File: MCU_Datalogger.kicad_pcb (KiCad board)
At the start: 2 copper layers, 0 parts

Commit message: setup for the 2layer PCB schematic
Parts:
- added BT1: Battery, Connector_PinHeader_2.54mm:PinHeader_1x02_P2.54mm_Vertical, F.Cu at (156.8, 101.4)
- added C1: 0.1 uF, Capacitor_SMD:C_0805_2012Metric, F.Cu at (179.1, 91.3)
- added C2: 22 pF, Capacitor_SMD:C_0805_2012Metric, F.Cu at (179.1, 94.4)
- added C3: 22 pF, Capacitor_SMD:C_0805_2012Metric, F.Cu at (179.1, 97.4)
- added C4: 0.1 uF, Capacitor_SMD:C_0805_2012Metric, F.Cu at (179.1, 100.4)
- added C5: 100 nF, Capacitor_SMD:C_0805_2012Metric, F.Cu at (179.1, 103.4)
- added D1: LED, LED_SMD:LED_0805_2012Metric, F.Cu at (183.5, 91.4)
- added D2: LED, LED_SMD:LED_0805_2012Metric, F.Cu at (183.5, 94.4)
- added H1: MountingHole, MountingHole:MountingHole_2.1mm, F.Cu at (157.3, 79.0)
- added H2: MountingHole, MountingHole:MountingHole_2.1mm, F.Cu at (157.3, 84.8)
- added H3: MountingHole, MountingHole:MountingHole_2.1mm, F.Cu at (157.3, 90.5)
- added H4: MountingHole, MountingHole:MountingHole_2.1mm, F.Cu at (157.3, 96.3)
- added J1: Conn_01x04_Pin, Connector_PinHeader_2.54mm:PinHeader_1x04_P2.54mm_Vertical, F.Cu at (194.6, 78.4)
- added J2: Conn_01x04_Pin, Connector_PinHeader_2.54mm:PinHeader_1x04_P2.54mm_Vertical, F.Cu at (199.2, 78.4)
- added J3: Conn_01x09_Pin, Connector_PinHeader_2.54mm:PinHeader_1x09_P2.54mm_Vertical, F.Cu at (190.0, 78.4)
- added J4: Conn_02x03_Odd_Even, Connector_PinHeader_2.54mm:PinHeader_2x03_P2.54mm_Vertical, F.Cu at (194.6, 90.6)
- added R1: 10k, Resistor_SMD:R_0805_2012Metric, F.Cu at (162.4, 77.6)
- added R2: 10 kOhm, Resistor_SMD:R_0805_2012Metric, F.Cu at (162.4, 80.6)
- added R3: 4.7 kOhm, Resistor_SMD:R_0805_2012Metric, F.Cu at (162.4, 83.5)
- added R4: 4.7 kOhm, Resistor_SMD:R_0805_2012Metric, F.Cu at (162.4, 86.5)
- added R5: 330 Ohm, Resistor_SMD:R_0805_2012Metric, F.Cu at (162.4, 89.4)
- added R6: 10 kOhm, Resistor_SMD:R_0805_2012Metric, F.Cu at (162.4, 92.4)
- added R7: 330 Ohm, Resistor_SMD:R_0805_2012Metric, F.Cu at (162.4, 95.3)
- added U1: 24LC1025, Package_SO:SOIC-8_5.3x5.3mm_P1.27mm, F.Cu at (169.8, 79.6)
- added U2: DS1337S_, Footprints:SOIC127P600X175-8N, F.Cu at (169.8, 104.5)
- added U3: 24LC1025, Package_SO:SOIC-8_5.3x5.3mm_P1.27mm, F.Cu at (169.8, 86.4)
- added U4: ATMEGA328P-AU, Footprints:QFP80P900X900X120-32N, F.Cu at (171.2, 95.5)
- added Y1: 32.768 KHz, Crystal:Crystal_SMD_5032-2Pin_5.0x3.2mm_HandSoldering, F.Cu at (180.1, 78.8)
- added Y2: 16 MHz, Crystal:Crystal_SMD_5032-2Pin_5.0x3.2mm_HandSoldering, F.Cu at (180.1, 84.0)

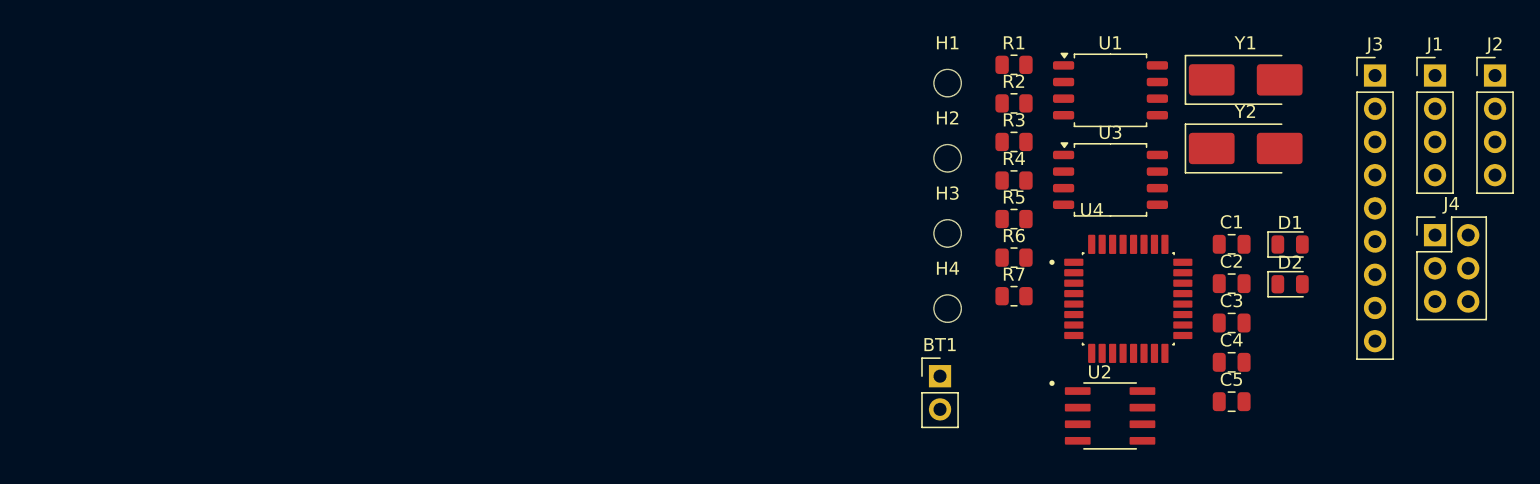
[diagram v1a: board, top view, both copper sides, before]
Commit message: Placing components on the PCB
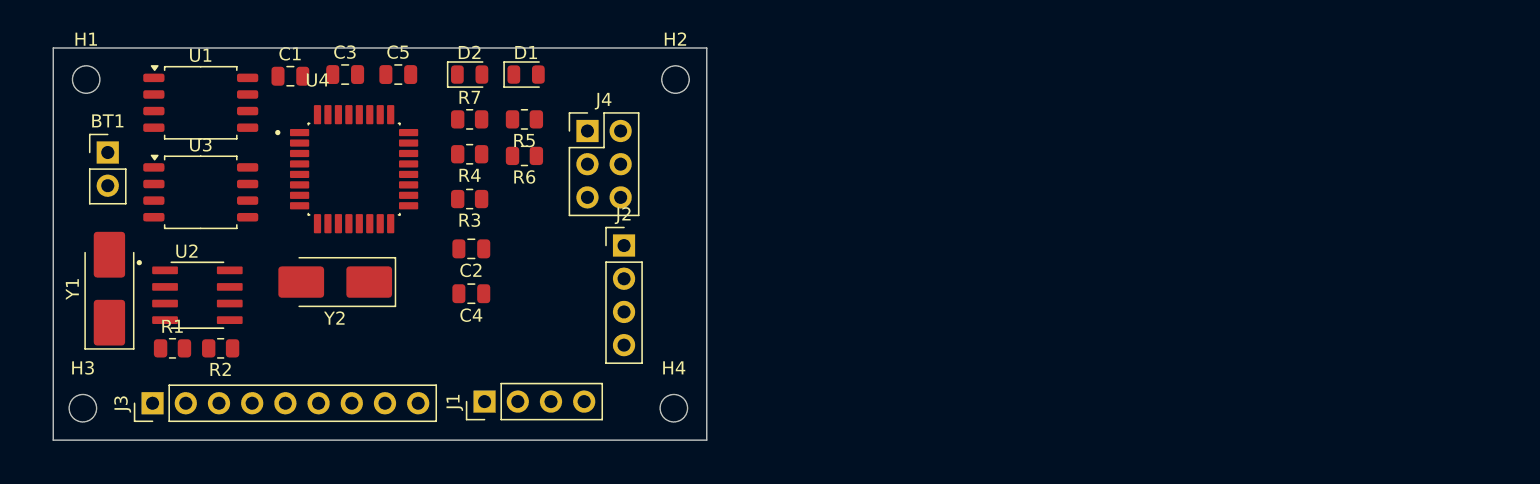
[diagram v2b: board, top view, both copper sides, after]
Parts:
- moved J3 96.8 mm to (96.5, 103.5), turned to 90 degrees
- moved Y1 88.4 mm to (93.2, 94.7), turned to 90 degrees
- moved J1 76.9 mm to (121.9, 103.4), turned to 90 degrees
- moved C1 73.2 mm to (107.1, 78.5)
- moved C3 70.4 mm to (111.3, 78.4)
- moved U2 70.4 mm to (99.9, 95.2)
- moved Y2 70.4 mm to (110.5, 94.2), turned to 180 degrees
- moved U1 69.6 mm to (100.2, 80.5)
- moved U3 69.6 mm to (100.2, 87.4)
- moved C5 68.5 mm to (115.3, 78.4)
- moved R1 67.9 mm to (98.0, 99.3)
- moved J2 67.9 mm to (132.6, 91.4)
- moved H3 67.5 mm to (91.2, 103.9)
- moved BT1 65.9 mm to (93.1, 84.3)
- moved H1 65.9 mm to (91.4, 78.7)
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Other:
- board outline added: 50 x 30 mm

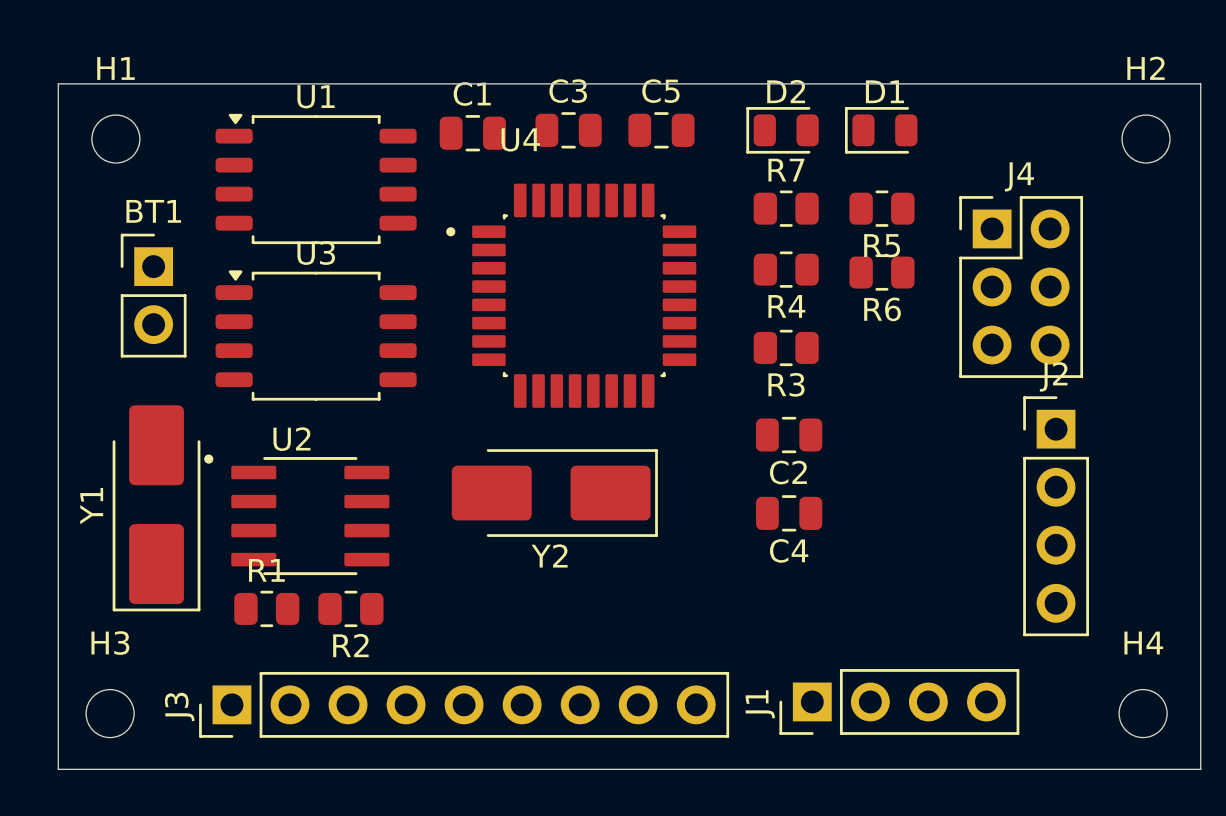
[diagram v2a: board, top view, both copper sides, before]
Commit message: routing components on PCB (still need fills for power and GND)
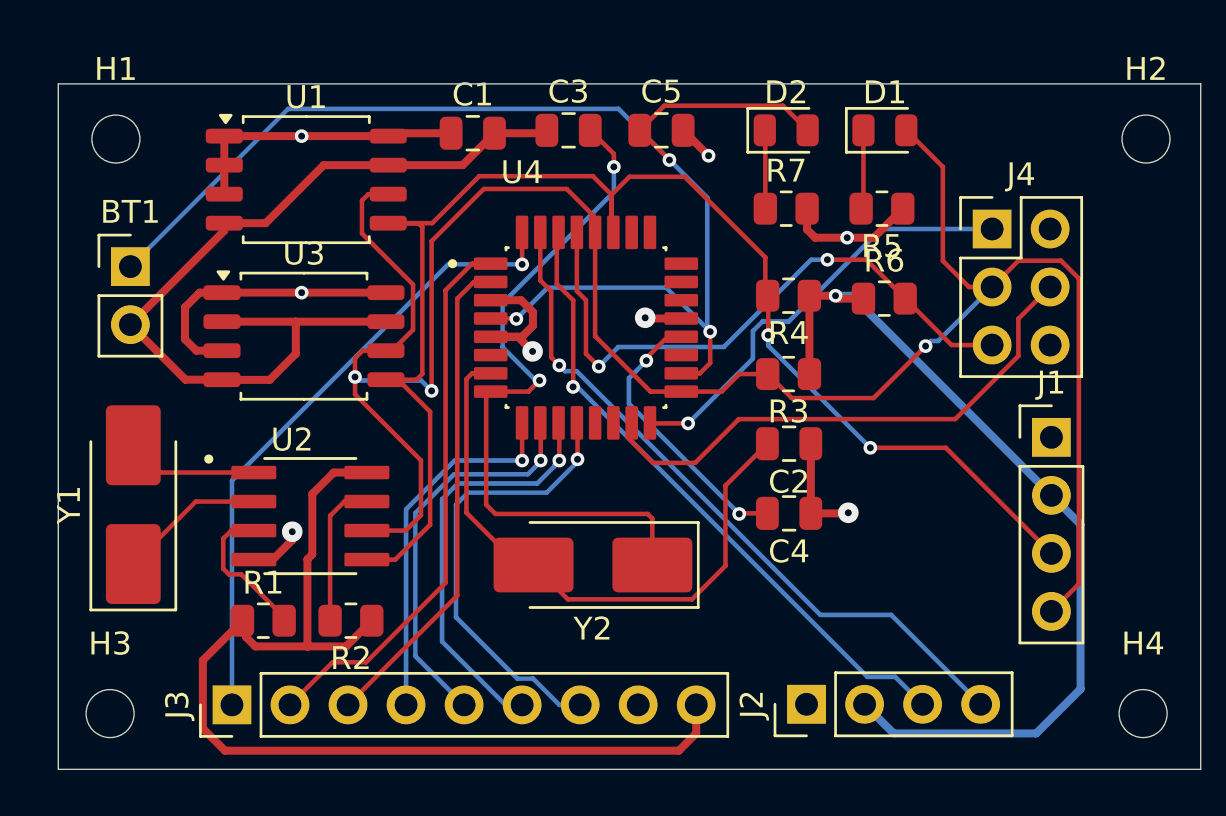
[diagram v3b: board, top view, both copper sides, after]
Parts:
- moved J2 16.3 mm to (121.7, 103.5), turned to 90 degrees
- moved J1 15.6 mm to (132.4, 91.8), turned to 0 degrees
- moved Y2 3.64 mm to (112.3, 97.4)
- moved U4 1.40 mm to (112.0, 87.0)
- moved R3 1.15 mm to (120.9, 89.0)
- moved R4 1.15 mm to (120.9, 85.6)
- moved R6 1.15 mm to (125.1, 85.7), turned to 0 degrees
- moved Y1 1.02 mm to (92.2, 94.7)
- moved BT1 1.02 mm to (92.1, 84.3)
- moved R1 0.54 mm to (97.9, 99.8)
- moved U3 0.53 mm to (99.7, 87.4)
- moved R2 0.52 mm to (101.7, 99.8)
- moved U1 0.43 mm to (99.8, 80.5)
- moved C2 0.38 mm to (120.9, 92.1)
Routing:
- net /Vcc: track 0.00 -> 109.2 mm, vias 0 -> 3
- net /SCK: track 0.00 -> 95.4 mm, vias 0 -> 3
- net /SDA: track 0.00 -> 63.4 mm, vias 0 -> 2
- net GND: track 0.00 -> 62.3 mm, vias 0 -> 6
- net Net-(BT1-+): track 0.00 -> 59.6 mm, vias 0 -> 3
- net Net-(U4-PB7): track 0.00 -> 31.5 mm, vias 0 -> 2
- net /TX: track 0.00 -> 30.8 mm, vias 0 -> 1
- net /RX: track 0.00 -> 28.2 mm, vias 0 -> 1
- net /D2: track 0.00 -> 27.8 mm, vias 0 -> 1
- net Net-(U4-PB6): track 0.00 -> 27.4 mm
- net /RESET: track 0.00 -> 27.0 mm, vias 0 -> 2
- net /D3: track 0.00 -> 24.3 mm
- net /MOSI: track 0.00 -> 23.7 mm
- net /D4: track 0.00 -> 21.5 mm
- net /D8: track 0.00 -> 19.8 mm, vias 0 -> 1
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
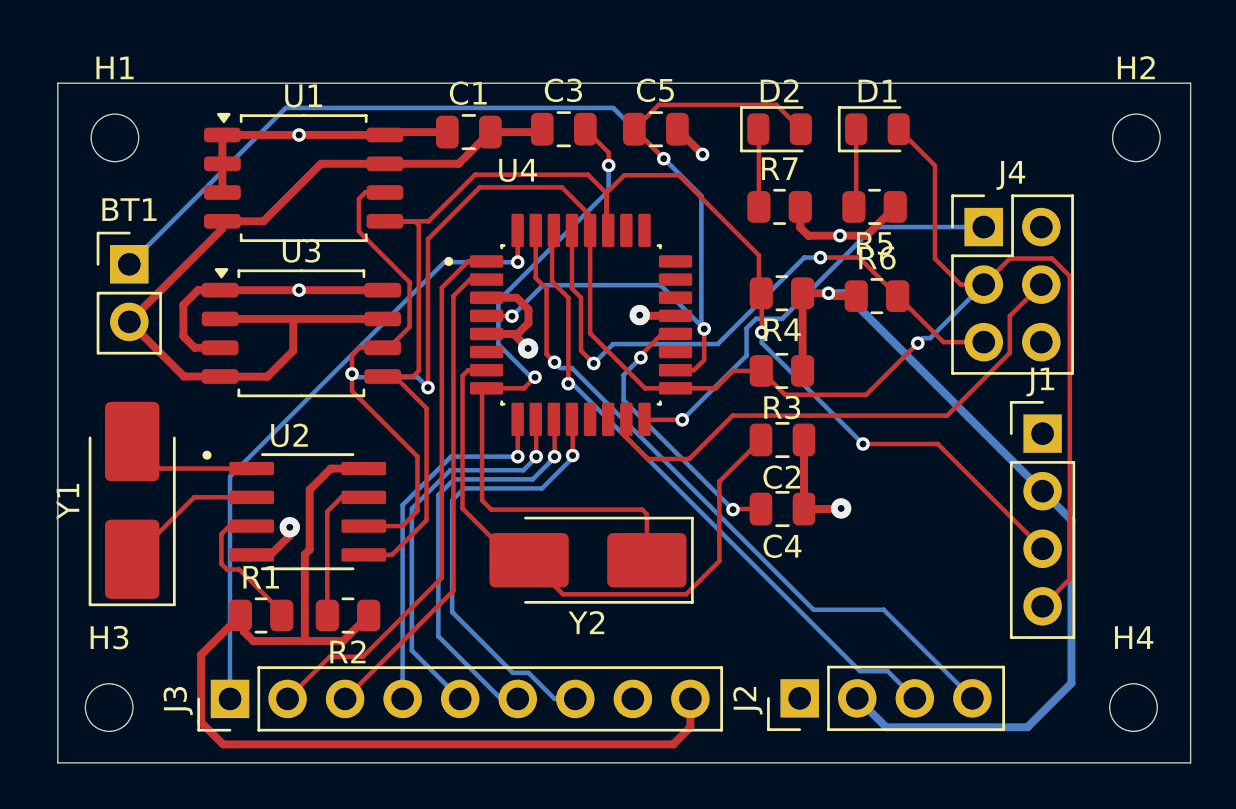
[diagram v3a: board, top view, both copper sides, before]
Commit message: adding fills to PCB
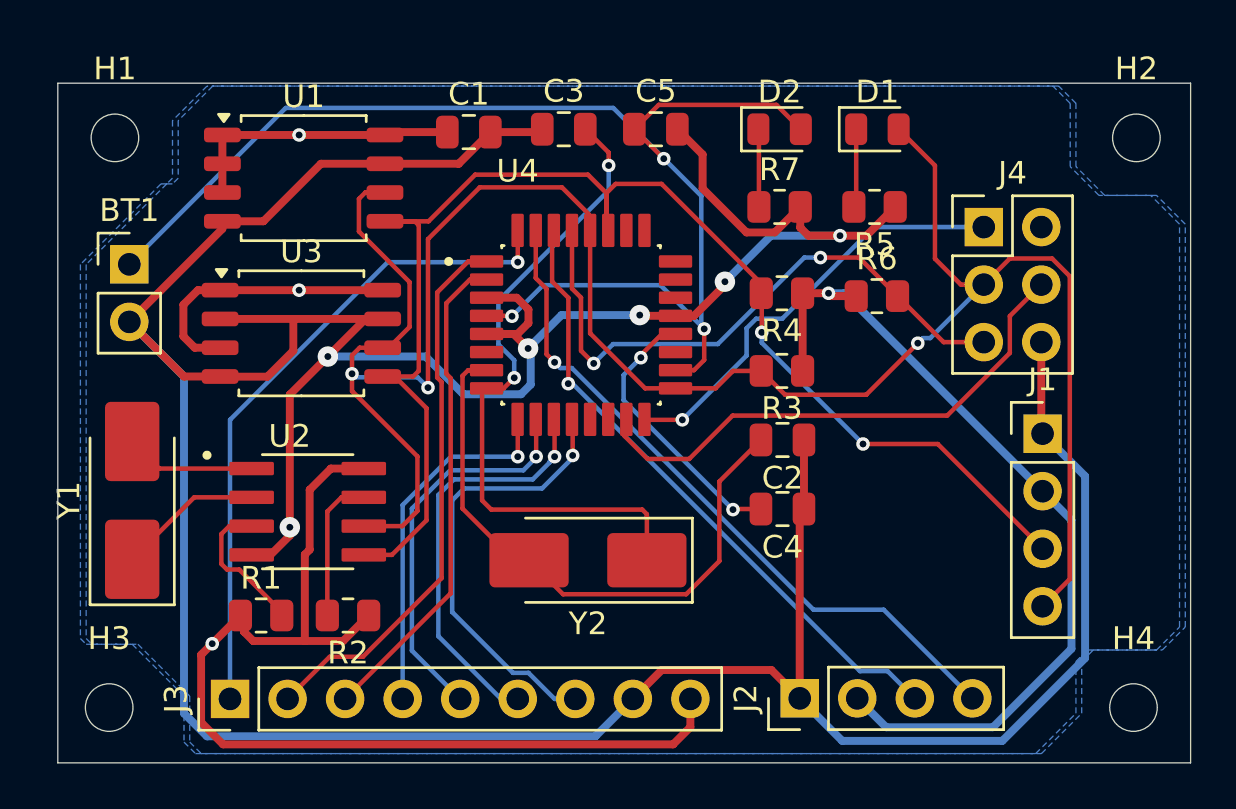
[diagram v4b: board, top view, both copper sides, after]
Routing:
- net GND: track 62.3 -> 190.5 mm
- net /D2: track 27.8 -> 29.3 mm
- net Net-(U4-PB7): track 31.5 -> 30.1 mm
- net /SDA: track 63.4 -> 62.4 mm
- net /Vcc: track 109.2 -> 108.3 mm, vias 3 -> 4
- added copper zone on B.Cu, net /Vcc
- added copper zone on B.Cu, net GND

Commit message: fixed silkscreen issues
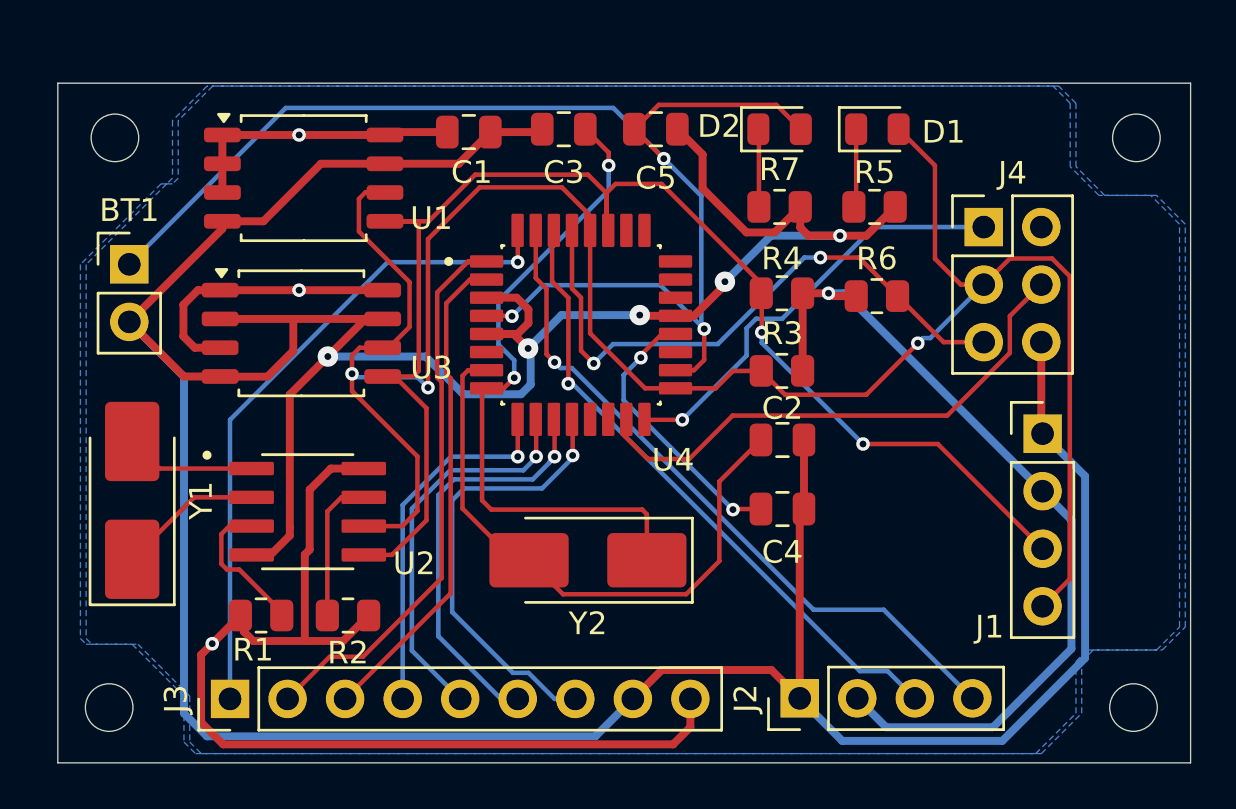
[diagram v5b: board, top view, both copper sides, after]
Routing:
- net GND: vias 6 -> 5
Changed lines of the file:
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@@
 		(at 112.014 86.995)
 		(property "Reference" "U4"
-			(at -2.795 -6.79 0)
+			(at 4.064 5.969 0)
 			(layer "F.SilkS")
 			(effects
@@
 			(at 0 -3.05 0)
 			(layer "F.SilkS")
+			(hide yes)
 			(effects
 				(font
@@
 		(tags "capacitor")
 		(property "Reference" "C3"
-			(at 0 -1.68 0)
+			(at 0 1.905 0)
 			(layer "F.SilkS")
 			(effects
@@
 		(tags "capacitor")
 		(property "Reference" "C4"
-			(at 0 -1.68 0)
+			(at 0 -1.905 0)
 			(layer "F.SilkS")
 			(effects
@@
 		(tags "capacitor")
 		(property "Reference" "C1"
-			(at 0 -1.68 0)
+			(at 0.127 1.778 0)
 			(layer "F.SilkS")
 			(effects
@@
 		(tags "SOIC SO P-SOP SOP SOP-8 SO SO-8 8S2 S2AE/F K04-056 CASE-751BE SO8W 8-Pin-SOIC PSA W8-2 W8-4 W8MS-1 FPT-8P-M08")
 		(property "Reference" "U3"
-			(at 0 -3.6 0)
+			(at 5.7404 1.532 0)
 			(layer "F.SilkS")
 			(effects
@@
 		(tags "resistor")
 		(property "Reference" "R5"
-			(at 0 -1.65 0)
+			(at 0 1.524 0)
 			(layer "F.SilkS")
 			(effects
@@
 			(at 0 -3.05 0)
 			(layer "F.SilkS")
+			(hide yes)
 			(effects
 				(font
@@
 		(at 99.949 95.242)
 		(property "Reference" "U2"
-			(at -0.795 -3.332 0)
+			(at 4.699 2.294 0)
 			(layer "F.SilkS")
 			(effects
@@
 		(tags "Through hole pin header THT 1x04 2.54mm single row")
 		(property "Reference" "J1"
-			(at 0 -2.38 0)
+			(at -2.3368 8.5344 0)
 			(layer "F.SilkS")
 			(effects
@@
 		(tags "resistor")
 		(property "Reference" "R3"
-			(at 0 -1.65 0)
+			(at -0.0235 1.651 0)
 			(layer "F.SilkS")
 			(effects
@@
 		(tags "resistor")
 		(property "Reference" "R1"
-			(at 0 -1.65 0)
+			(at -0.3556 1.524 0)
 			(layer "F.SilkS")
 			(effects
@@
 			(at 0 -3.05 0)
 			(layer "F.SilkS")
+			(hide yes)
 			(effects
 				(font
@@
 			(at 0 -3.05 0)
 			(layer "F.SilkS")
+			(hide yes)
 			(effects
 				(font
@@
 		(tags "capacitor")
 		(property "Reference" "C5"
-			(at 0 -1.68 0)
+			(at 0 2.159 0)
 			(layer "F.SilkS")
 			(effects
@@
 		(tags "capacitor")
 		(property "Reference" "C2"
-			(at 0 -1.68 0)
+			(at 0 1.397 0)
 			(layer "F.SilkS")
 			(effects
@@
 		(tags "LED")
 		(property "Reference" "D1"
-			(at 0 -1.65 0)
+			(at 2.921 0.127 0)
 			(layer "F.SilkS")
 			(effects
@@
 		(tags "SOIC SO P-SOP SOP SOP-8 SO SO-8 8S2 S2AE/F K04-056 CASE-751BE SO8W 8-Pin-SOIC PSA W8-2 W8-4 W8MS-1 FPT-8P-M08")
 		(property "Reference" "U1"
-			(at 0 -3.6 0)
+			(at 5.6388 1.778 0)
 			(layer "F.SilkS")
 			(effects
@@
 		(descr "SMD2520/2, Crystal, 5.0x3.2mm package, SMD, hand-soldering, generated with kicad-footprint-generator make_crystal.py, http://www.icbase.com/File/PDF/HKC/HKC00061008.pdf")
 		(property "Reference" "Y1"
-			(at 0 -2.8 90)
+			(at 0 3.048 90)
 			(layer "F.SilkS")
 			(effects
@@
 		(tags "LED")
 		(property "Reference" "D2"
-			(at 0 -1.65 0)
+			(at -2.667 -0.127 0)
 			(layer "F.SilkS")
 			(effects
@@
 		(tags "resistor")
 		(property "Reference" "R4"
-			(at 0 -1.65 0)
+			(at 0 1.524 0)
 			(layer "F.SilkS")
 			(effects
@@
 		(size 0.9)
 		(drill 0.3)
-		(layers "F.Cu" "B.Cu")
-		(net 1)
-	)
-	(via
-		(at 99.159 95.927252)
-		(size 0.9)
-		(drill 0.3)

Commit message: fixed silkscreen issues pt2
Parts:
- R1: value 10k -> 10kOhm
